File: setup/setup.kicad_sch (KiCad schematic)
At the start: 19 parts, among them J1 Conn_01x08_Socket, J11 Motor Power, J2 Conn_01x08_Socket, J3 Step M1, J4 PS2 Controller, J5 Conn_01x22_Socket, J6 Conn_01x22_Socket, J7 6V IN, J8 Additional Outputs, M1 Motor_Servo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

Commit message: feat: add oled(pcb)
Signed-off-by: kyle <kyle@nixos-portable>
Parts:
- added U1: ER_OLEDM0.91_1x-I2C, Connector_JST:JST_XH_S4B-XH-A-1_1x04_P2.50mm_Horizontal, symbol Display_Graphic:ER_OLEDM0.91_1x-I2C
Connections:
- net GND: now also U1.1 (GND)
- net at J2.7 (VDD), J5.1 (3V3): now also U1.2 (VCC)
- net at J6.4 (1): now also U1.3 (SCL)
- net at J6.5 (2): now also U1.4 (SDA)
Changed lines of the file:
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@@
 		(color 0 0 0 0)
 	)
+	(junction
+		(at 124.46 87.63)
+		(diameter 0)
+		(color 0 0 0 0)
+	)
 	(wire
 		(pts
@@
 	(wire
 		(pts
+			(xy 132.08 102.87) (xy 127 102.87)
+		)
+		(stroke
+			(width 0)
+			(type default)
+		)
+	)
+	(wire
+		(pts
 			(xy 120.65 68.58) (xy 123.19 68.58)
 		)
@@
 	(wire
 		(pts
+			(xy 116.84 102.87) (xy 124.46 102.87)
+		)
+		(stroke
+			(width 0)
+			(type default)
+		)
+	)
+	(wire
+		(pts
 			(xy 68.58 130.81) (xy 68.58 143.51)
 		)
@@
 	(wire
 		(pts
+			(xy 142.24 87.63) (xy 124.46 87.63)
+		)
+		(stroke
+			(width 0)
+			(type default)
+		)
+	)
+	(wire
+		(pts
 			(xy 46.99 34.29) (xy 46.99 40.64)
 		)
@@
 	(wire
 		(pts
+			(xy 124.46 102.87) (xy 124.46 107.95)
+		)
+		(stroke
+			(width 0)
+			(type default)
+		)
+	)
+	(wire
+		(pts
+			(xy 142.24 95.25) (xy 142.24 87.63)
+		)
+		(stroke
+			(width 0)
+			(type default)
+		)
+	)
+	(wire
+		(pts
 			(xy 77.47 154.94) (xy 77.47 143.51)
 		)
@@
 	(wire
 		(pts
+			(xy 124.46 107.95) (xy 132.08 107.95)
+		)
+		(stroke
+			(width 0)
+			(type default)
+		)
+	)
+	(wire
+		(pts
 			(xy 81.28 76.2) (xy 81.28 78.74)
 		)
@@
 	(wire
 		(pts
+			(xy 116.84 100.33) (xy 127 100.33)
+		)
+		(stroke
+			(width 0)
+			(type default)
+		)
+	)
+	(wire
+		(pts
 			(xy 81.28 118.11) (xy 38.1 118.11)
 		)
@@
 	(wire
 		(pts
+			(xy 127 102.87) (xy 127 100.33)
+		)
+		(stroke
+			(width 0)
+			(type default)
+		)
+	)
+	(wire
+		(pts
 			(xy 165.1 154.94) (xy 77.47 154.94)
 		)
@@
 	)
 	(symbol
+		(lib_id "Display_Graphic:ER_OLEDM0.91_1x-I2C")
+		(at 142.24 105.41 0)
+		(unit 1)
+		(body_style 1)
+		(exclude_from_sim no)
+		(in_bom yes)
+		(on_board yes)
+		(in_pos_files yes)
+		(dnp no)
+		(fields_autoplaced yes)
+		(property "Reference" "U1"
+			(at 151.13 104.1399 0)
+			(show_name no)
+			(do_not_autoplace no)
+			(effects
+				(font
+					(size 1.27 1.27)
+				)
+				(justify left)
+			)
+		)
+		(property "Value" "ER_OLEDM0.91_1x-I2C"
+			(at 151.13 106.6799 0)
+			(show_name no)
+			(do_not_autoplace no)
+			(effects
+				(font
+					(size 1.27 1.27)
+				)
+				(justify left)
+			)
+		)
+		(property "Footprint" "Connector_JST:JST_XH_S4B-XH-A-1_1x04_P2.50mm_Horizontal"
+			(at 160.274 118.11 0)
+			(hide yes)
+			(show_name no)
+			(do_not_autoplace no)
+			(effects
+				(font
+					(size 1.27 1.27)
+				)
+			)
+		)
+		(property "Datasheet" "https://www.buydisplay.com/download/manual/ER-OLEDM0.91-1_Datasheet.pdf"
+			(at 184.912 120.142 0)
+			(hide yes)
+			(show_name no)
+			(do_not_autoplace no)
+			(effects
+				(font
+					(size 1.27 1.27)
+				)
+			)
+		)
+		(property "Description" "SSD1306 OLED module, 0.91 inch, 128x32, I2C"
+			(at 168.91 122.174 0)
+			(hide yes)
+			(show_name no)
+			(do_not_autoplace no)
+			(effects
+				(font
+					(size 1.27 1.27)
+				)
+			)
+		)
+		(pin "4"
+		)
+		(pin "3"
+		)
+		(pin "2"
+		)
+		(pin "1"
+		)
+		(instances
+			(project "setup"
+				(path "/0961cb8e-9a33-475b-99c1-b45e6599961f"
+					(reference "U1")
+					(unit 1)
+				)
+			)
+		)
+	)
+	(symbol
 		(lib_id "Connector_Generic:Conn_01x04")
 		(at 125.73 73.66 0)
@@
 					(unit 1)
 				)
+			)
+		)
+	)
+	(symbol
+		(lib_id "power:GND")
+		(at 142.24 115.57 0)
+		(unit 1)
+		(body_style 1)
+		(exclude_from_sim no)
+		(in_bom yes)
+		(on_board yes)
+		(in_pos_files yes)
+		(dnp no)
+		(fields_autoplaced yes)
+		(property "Reference" "#PWR015"
+			(at 142.24 121.92 0)
+			(hide yes)
+			(show_name no)
+			(do_not_autoplace no)
+			(effects
+				(font
+					(size 1.27 1.27)
+				)
+			)
+		)
+		(property "Value" "GND"
+			(at 142.24 120.65 0)
+			(show_name no)
+			(do_not_autoplace no)
+			(effects
+				(font
+					(size 1.27 1.27)
+				)
+			)
+		)
+		(property "Footprint" ""
+			(at 142.24 115.57 0)
+			(hide yes)
+			(show_name no)
+			(do_not_autoplace no)
+			(effects
+				(font
+					(size 1.27 1.27)
+				)
+			)
+		)
+		(property "Datasheet" ""
+			(at 142.24 115.57 0)
+			(hide yes)
+			(show_name no)
+			(do_not_autoplace no)
+			(effects
+				(font
+					(size 1.27 1.27)
+				)
+			)
+		)
+		(property "Description" "Power symbol creates a global label with name \"GND\" , ground"
+			(at 142.24 115.57 0)
+			(hide yes)
+			(show_name no)
+			(do_not_autoplace no)
+			(effects
+				(font
+					(size 1.27 1.27)
+				)
+			)
+		)
+		(pin "1"
+		)
+		(instances
+			(project "setup"
+				(path "/0961cb8e-9a33-475b-99c1-b45e6599961f"
+					(reference "#PWR015")
+					(unit 1)
+				)

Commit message: feat: re-order pcb
Signed-off-by: kyle <kyle@nixos-desktop>
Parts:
- removed J8: Additional Outputs, Connector_PinSocket_2.54mm:PinSocket_1x08_P2.54mm_Vertical, symbol Connector:Conn_01x08_Socket
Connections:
- net GND: now also C1.2; no longer U1.1 (GND)
- net at C1.1, J11.1 (12V), Jf1.1 (VOUT): now also J2.1 (VMOTOR)
- net at J5.21 (5VIn), J7.1 (VIN), M1.2 (+)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: no longer J4.2 (VCC)
- net at J2.7 (VDD), J5.1 (3V3), U1.2 (VCC): now also J4.2 (VCC)

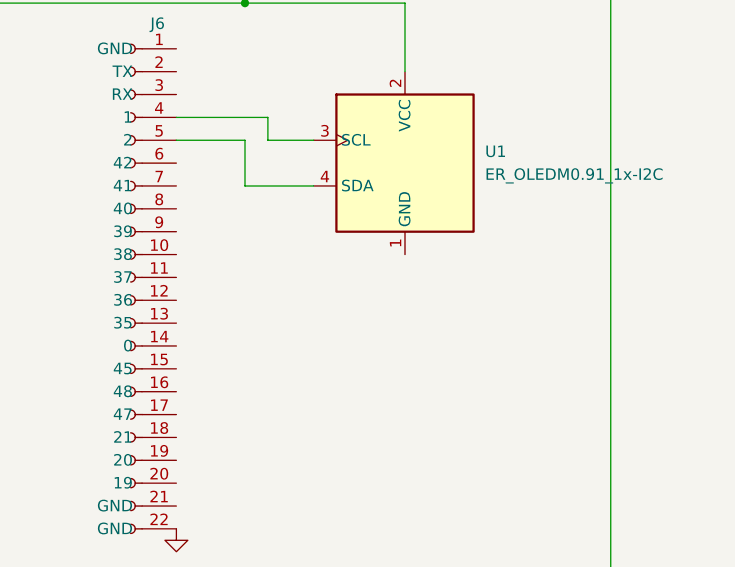
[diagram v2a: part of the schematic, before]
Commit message: feat: use two-layer routing for motor voltages
Signed-off-by: kyle <kyle@nixos-desktop>
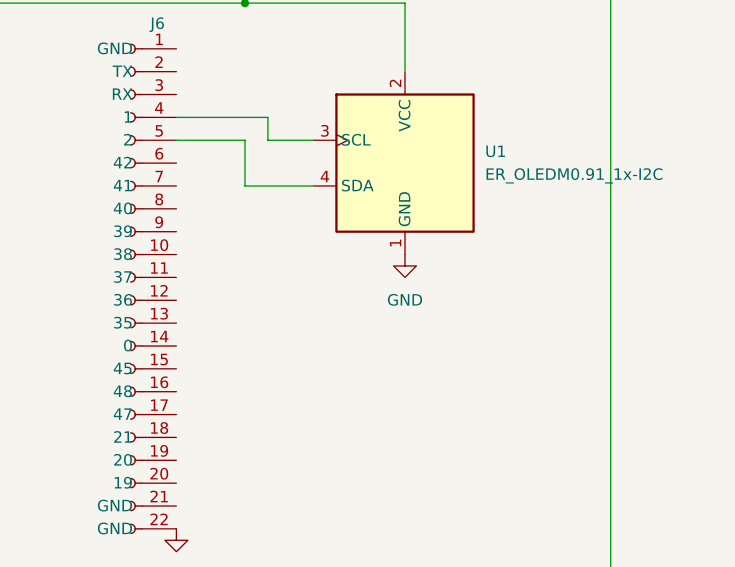
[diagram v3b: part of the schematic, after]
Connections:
- net GND: now also U1.1 (GND)
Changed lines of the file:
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@@
+	)
+	(symbol
+		(lib_id "power:GND")
+		(at 142.24 115.57 0)
+		(unit 1)
+		(body_style 1)
+		(exclude_from_sim no)
+		(in_bom yes)
+		(on_board yes)
+		(in_pos_files yes)
+		(dnp no)
+		(fields_autoplaced yes)
+		(property "Reference" "#PWR016"
+			(at 142.24 121.92 0)
+			(hide yes)
+			(show_name no)
+			(do_not_autoplace no)
+			(effects
+				(font
+					(size 1.27 1.27)
+				)
+			)
+		)
+		(property "Value" "GND"
+			(at 142.24 120.65 0)
+			(show_name no)
+			(do_not_autoplace no)
+			(effects
+				(font
+					(size 1.27 1.27)
+				)
+			)
+		)
+		(property "Footprint" ""
+			(at 142.24 115.57 0)
+			(hide yes)
+			(show_name no)
+			(do_not_autoplace no)
+			(effects
+				(font
+					(size 1.27 1.27)
+				)
+			)
+		)
+		(property "Datasheet" ""
+			(at 142.24 115.57 0)
+			(hide yes)
+			(show_name no)
+			(do_not_autoplace no)
+			(effects
+				(font
+					(size 1.27 1.27)
+				)
+			)
+		)
+		(property "Description" "Power symbol creates a global label with name \"GND\" , ground"
+			(at 142.24 115.57 0)
+			(hide yes)
+			(show_name no)
+			(do_not_autoplace no)
+			(effects
+				(font
+					(size 1.27 1.27)
+				)
+			)
+		)
+		(pin "1"
+		)
+		(instances
+			(project "setup"
+				(path "/0961cb8e-9a33-475b-99c1-b45e6599961f"
+					(reference "#PWR016")
+					(unit 1)
+				)
+			)
+		)
 	)
 	(symbol

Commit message: feat: make board jlcpcb compatiable
Signed-off-by: kyle <kyle@nixos-desktop>
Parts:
- J7: footprint Connector_JST:JST_PH_B2B-PH-K_1x02_P2.00mm_Vertical -> Connector_JST:JST_XH_B2B-XH-A_1x02_P2.50mm_Vertical
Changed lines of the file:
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@@
 			)
 		)
-		(property "Footprint" "Connector_JST:JST_PH_B2B-PH-K_1x02_P2.00mm_Vertical"
+		(property "Footprint" "Connector_JST:JST_XH_B2B-XH-A_1x02_P2.50mm_Vertical"
 			(at 165.1 38.1 0)
 			(hide yes)

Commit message: feat: add jlcpcb & fix vh connection
Signed-off-by: kyle <kyle@nixos-portable>
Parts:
- J11, Jf1: footprint Connector_JST:JST_PH_B2B-PH-K_1x02_P2.00mm_Vertical -> Connector_JST:JST_VH_B2P-VH-FB-B_1x02_P3.96mm_Vertical
- J7: footprint Connector_JST:JST_XH_B2B-XH-A_1x02_P2.50mm_Vertical -> Connector_JST:JST_VH_B2P-VH-FB-B_1x02_P3.96mm_Vertical
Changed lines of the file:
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@@
 			)
 		)
-		(property "Footprint" "Connector_JST:JST_PH_B2B-PH-K_1x02_P2.00mm_Vertical"
+		(property "Footprint" "Connector_JST:JST_VH_B2P-VH-FB-B_1x02_P3.96mm_Vertical"
 			(at 138.43 26.67 0)
 			(hide yes)
@@
 			)
 		)
-		(property "Footprint" "Connector_JST:JST_PH_B2B-PH-K_1x02_P2.00mm_Vertical"
+		(property "Footprint" "Connector_JST:JST_VH_B2P-VH-FB-B_1x02_P3.96mm_Vertical"
 			(at 148.59 34.29 0)
 			(hide yes)
@@
 			)
 		)
-		(property "Footprint" "Connector_JST:JST_XH_B2B-XH-A_1x02_P2.50mm_Vertical"
+		(property "Footprint" "Connector_JST:JST_VH_B2P-VH-FB-B_1x02_P3.96mm_Vertical"
 			(at 165.1 38.1 0)
 			(hide yes)
